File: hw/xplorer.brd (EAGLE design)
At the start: 105 x 60 mm, 112 parts, among them T2 BC817, T5 ZDT6790, U1 PCM5102APW, U2 BMP085, U3 AD8345, U4 MIC5233, U5 MAX2614, U6 RA08H1317M, U7 TPS7A4901, U8 MAX4478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

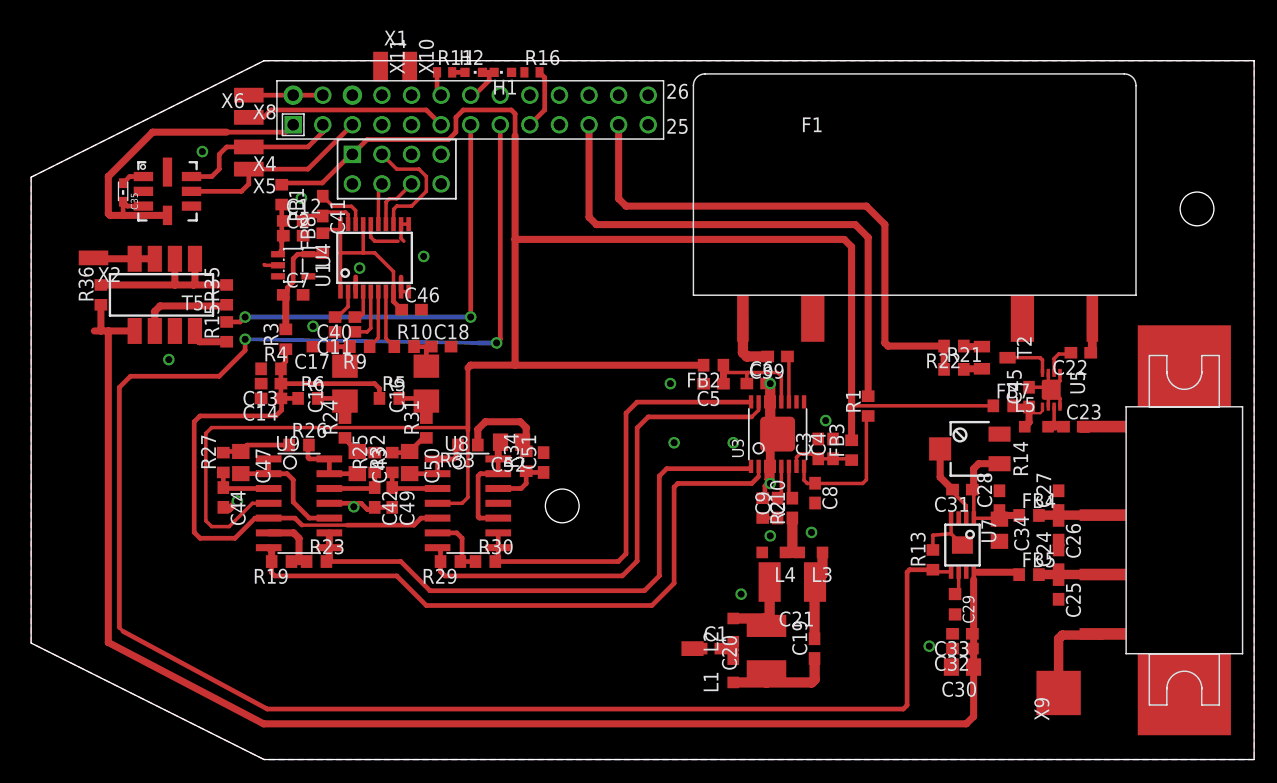
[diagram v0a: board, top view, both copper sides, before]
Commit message: correct pcb file structure
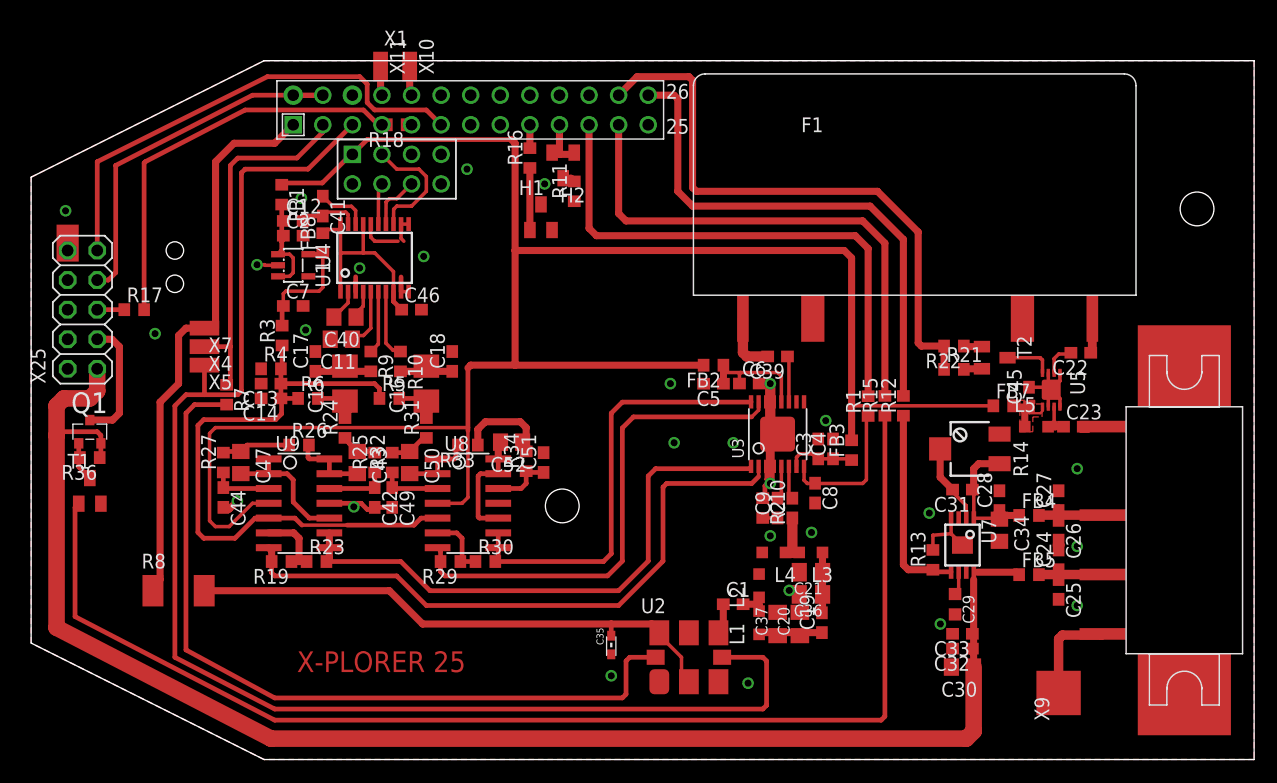
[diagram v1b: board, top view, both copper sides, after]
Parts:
- removed R35: 8k8, rcl:R0603
- removed T5: ZDT6790, ZDT6790:SOT223-8
- removed X2, X6, X8: (no value), wirepad:SMD1,27-2,54
- added C36, C37: 8p, rcl:C0805K
- added Q1: IRLML6402, transistor-power:MICRO3
- added R12, R7: (no value), rcl:R0603
- added R17: 475R, rcl:R0603
- added R18: 1k, rcl:R0603
- added R8: (no value), rcl:R2010
- added T1: (no value), transistor:SOT23-BEC
- added X25: (no value), pinhead:2X05
- added X7: (no value), wirepad:SMD1,27-2,54
- C11, C40: device rcl:C0603 -> rcl:C0805
- C20, C21: device rcl:C1812 -> rcl:C0805K
- H1, H2: device led:CHIPLED_0603 -> led:SOT23
- R11, R16: device rcl:R0402 -> rcl:R0603
- U2: value BMP085 -> SI570; device SparkFun:BMP085 -> silabs:8-PIN
- moved U2 60.0 mm to (34.0, -45.7)
- moved C35 57.3 mm to (27.3, -44.8), turned to 270 degrees
- moved R15 56.9 mm to (50.8, -24.1)
- moved X4 17.6 mm to (-7.62, -19.1)
- moved X5 17.3 mm to (-7.62, -20.6)
- moved R11 15.1 mm to (24.1, -5.71), turned to 90 degrees
- moved R36 14.0 mm to (-17.5, -28.6), turned to 180 degrees
- moved H1 12.9 mm to (21.3, -7.94), turned to 0 degrees
- moved H2 11.1 mm to (23.2, -3.49), turned to 180 degrees
- moved R16 7.36 mm to (20.3, -2.86), turned to 90 degrees
- moved L1 4.69 mm to (40.0, -42.8)
- moved L2 4.41 mm to (40.0, -39.6)
- moved C1 4.26 mm to (37.8, -41.2)
- moved C20 3.56 mm to (43.5, -42.9)
- moved C19 2.31 mm to (45.4, -42.8)
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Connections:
- removed net $234567898765: T5.3, T5.4, X2.1
- removed net N$31: R11.1, X1.P1_12
- removed net N$55: R35.1, T5.6
- new net HEAD: R17.1, X25.5
- new net N$13: R7.2, U2.7
- new net N$25: R12.1, R13.1, U7.5
- new net N$27: R17.2, R18.2, X1.P1_7
- new net REL: Q1.3, X25.3
- new net STAT: H2.1, X1.P1_19
- new net VLA: C19.1, C20.1, C37.1, L1.1
- net +12V: now also Q1.2, X25.1; no longer T5.5
- net +3V3: now also R8.1, X7.1; no longer C35.1, U2.3, U2.4
- net +5V: now also X25.7; no longer X8.1
- net GND: now also C36.2, C37.2, H1.3, R11.1, R18.1, T1.E, U2.3, X25.2, X25.4, X25.6, X25.8; no longer H1.C, H2.C, T5.7, U2.1
- net LO: now also U2.4; no longer X1.P1_7
- net N$14: now also C36.1
- net N$16: now also H2.3; no longer H2.A
- net N$18: now also H1.1; no longer H1.A
- net N$19: now also C35.1, R8.2, U2.2, U2.6; no longer C19.1, C20.1, L1.1
- net N$42: now also T1.B; no longer T5.8
- net N$54: now also Q1.1, T1.C; no longer R35.2, T5.1, T5.2
- net N$66: now also X1.P1_23; no longer X1.P1_13
- net PA_EN: now also R12.2, X1.P1_26; no longer R13.1, U7.5, X1.P1_15
- net PRE_EN: now also X1.P1_24; no longer X1.P1_23
- net REL_FB: now also X25.9; no longer X6.1
- net SCL: now also U2.8; no longer U2.6
- net SDA: now also R7.1; no longer U2.7
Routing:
- net PA_EN: track 159.1 -> 45.1 mm, vias 2 -> 0
- net N$42: track 3.41 -> 107.5 mm
- net SCL: track 16.9 -> 120.1 mm
- net N$13: track 0.00 -> 68.6 mm
- net N$19: track 9.86 -> 47.2 mm
- net N$27: track 0.00 -> 34.7 mm
- net REL_FB: track 17.3 -> 41.5 mm
- net +5V: track 180.4 -> 200.9 mm
- net N$25: track 0.00 -> 17.1 mm
- net SDA: track 14.2 -> 31.3 mm
- net +3V3: track 34.4 -> 50.5 mm
- net GND: track 64.9 -> 51.5 mm, vias 18 -> 27
- net N$54: track 15.3 -> 3.47 mm
- net REL: track 0.00 -> 10.7 mm
- net N$55: track 8.09 -> 0.00 mm
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- added copper zone on layer 1, net +5V_MAX
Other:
- board text added: "X-PLORER 25"
